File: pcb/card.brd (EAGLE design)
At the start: 69.5 x 40.6 mm, 21 parts, among them IC1 74HC14D, IC2 24LC256SN, Q1 BC817

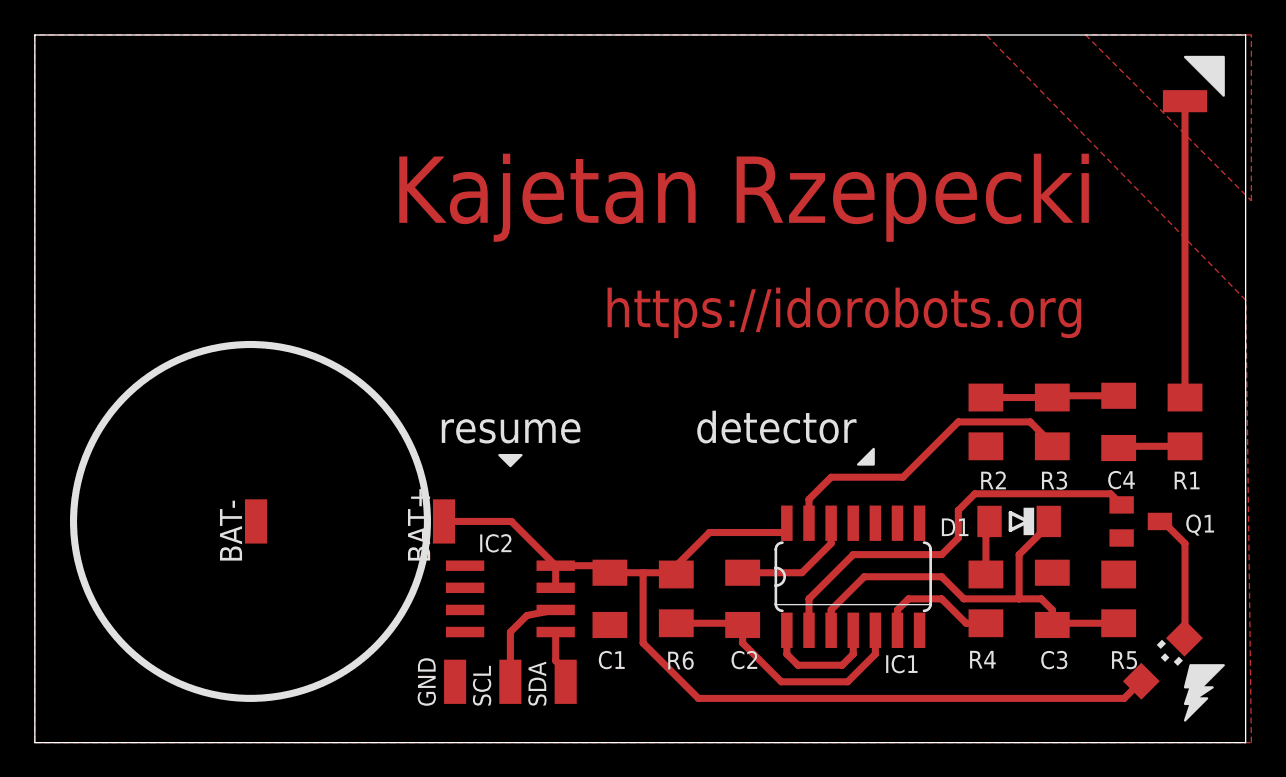
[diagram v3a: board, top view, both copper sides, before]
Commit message: Apparently 10M Ohm is as high as it gets for reasonable amount of money.
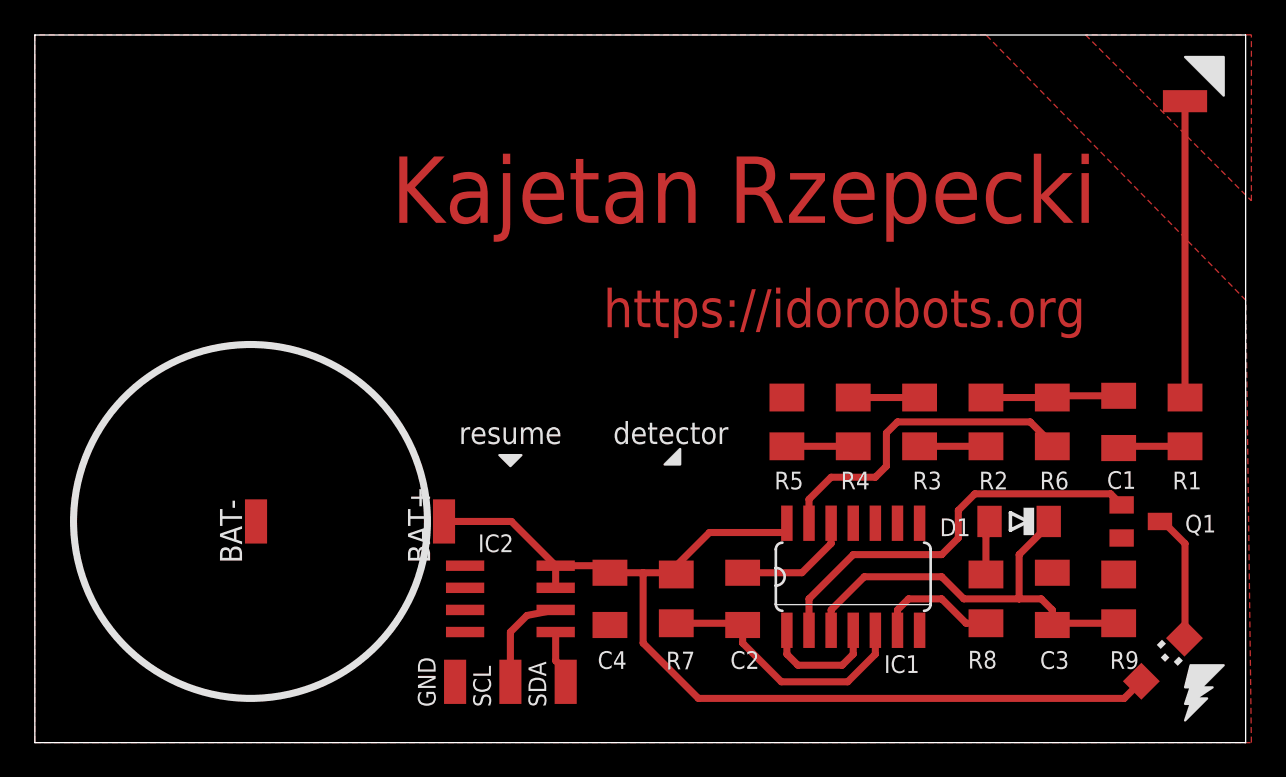
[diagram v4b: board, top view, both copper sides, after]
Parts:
- added R7, R9: 470k, resistor:M1206
- added R8: 100k, resistor:M1206
- R2: value 40M -> 10M
- R3, R5: value 470k -> 10M
- R4: value 100k -> 10M
- moved C1 30.9 mm to (62.2, 18.4)
- moved C4 30.9 mm to (33.0, 8.26)
- moved R6 23.9 mm to (58.4, 18.4)
- moved R5 21.6 mm to (43.2, 18.4), turned to 270 degrees
- moved R4 12.7 mm to (47.0, 18.4), turned to 90 degrees
- moved R3 7.62 mm to (50.8, 18.4), turned to 270 degrees
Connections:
- new net N$14: R2.1, R3.2
- new net N$15: R3.1, R4.2
- new net N$16: R4.1, R5.2
- net GND: now also C4.1, R5.1, R9.2; no longer C1.1, R2.1, R5.2
- net N$1: now also C1.1; no longer C4.1
- net N$2: now also C1.2, R6.2; no longer C4.2, R3.2
- net N$3: now also R6.1; no longer R3.1
- net N$5: now also R7.1; no longer R6.1
- net N$6: now also R8.2; no longer R4.2
- net N$7: now also R8.1; no longer R4.1
- net N$8: now also R9.1; no longer R5.1
- net VCC: now also C4.2, R7.2; no longer C1.2, R6.2
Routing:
- net N$16: track 0.00 -> 3.81 mm
- net N$14: track 0.00 -> 3.81 mm
- net N$15: track 0.00 -> 3.81 mm
- net N$3: track 18.8 -> 19.9 mm
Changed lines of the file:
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@@
 <setting verticaltext="up"/>
 </settings>
-<grid distance="0.3175" unitdist="mm" unit="mm" style="lines" multiple="1" display="no" altdistance="0.3175" altunitdist="mm" altunit="mm"/>
+<grid distance="0.635" unitdist="mm" unit="mm" style="lines" multiple="1" display="no" altdistance="0.3175" altunitdist="mm" altunit="mm"/>
 <layers>
 <layer number="1" name="Top" color="4" fill="1" visible="yes" active="yes"/>
@@
 <vertex x="27.94" y="16.51"/>
 </polygon>
-<text x="27.305" y="18.0975" size="1.778" layer="25" rot="R180" align="center">resume</text>
+<text x="27.305" y="17.78" size="1.27" layer="25" rot="R180" align="center">resume</text>
 <polygon width="0.127" layer="25">
-<vertex x="48.167003125" y="15.967996875"/>
-<vertex x="47.268975" y="15.96799375"/>
-<vertex x="48.167003125" y="16.866021875"/>
+<vertex x="37.054503125" y="15.967996875"/>
+<vertex x="36.156475" y="15.96799375"/>
+<vertex x="37.054503125" y="16.866021875"/>
 </polygon>
-<text x="42.545" y="18.0975" size="1.778" layer="25" rot="R180" align="center">detector</text>
+<text x="36.5125" y="17.78" size="1.27" layer="25" rot="R180" align="center">detector</text>
 </plain>
 <attributes>
@@
 </autorouter>
 <elements>
-<element name="C1" library="resistor" package="C1206K" value="10nF" x="33.02" y="8.255" smashed="yes" rot="R90">
+<element name="C4" library="resistor" package="C1206K" value="10nF" x="33.02" y="8.255" smashed="yes" rot="R90">
 <attribute name="NAME" x="33.985" y="5.25" size="1.016" layer="25" rot="R180"/>
 </element>
@@
 <attribute name="NAME" x="66.9925" y="15.5575" size="1.016" layer="25" rot="R180"/>
 </element>
-<element name="R2" library="resistor" package="M1206" value="40M" x="54.61" y="18.415" smashed="yes" rot="R90">
+<element name="R2" library="resistor" package="M1206" value="10M" x="54.61" y="18.415" smashed="yes" rot="R90">
 <attribute name="NAME" x="55.88" y="15.5575" size="1.016" layer="25" rot="R180"/>
 </element>
-<element name="R3" library="resistor" package="M1206" value="470k" x="58.42" y="18.415" smashed="yes" rot="R90">
+<element name="R6" library="resistor" package="M1206" value="470k" x="58.42" y="18.415" smashed="yes" rot="R90">
 <attribute name="NAME" x="59.3725" y="15.5575" size="1.016" layer="25" rot="R180"/>
 </element>
-<element name="R4" library="resistor" package="M1206" value="100k" x="54.61" y="8.255" smashed="yes" rot="R270">
+<element name="R8" library="resistor" package="M1206" value="100k" x="54.61" y="8.255" smashed="yes" rot="R270">
 <attribute name="NAME" x="55.245" y="5.2700625" size="1.016" layer="25" rot="R180"/>
 </element>
-<element name="R5" library="resistor" package="M1206" value="470k" x="62.23" y="8.255" smashed="yes" rot="R90">
+<element name="R9" library="resistor" package="M1206" value="470k" x="62.23" y="8.255" smashed="yes" rot="R90">
 <attribute name="NAME" x="63.39549375" y="5.251046875" size="1.016" layer="25" rot="R180"/>
 </element>
-<element name="R6" library="resistor" package="M1206" value="470k" x="36.83" y="8.255" smashed="yes" rot="R90">
+<element name="R7" library="resistor" package="M1206" value="470k" x="36.83" y="8.255" smashed="yes" rot="R90">
 <attribute name="NAME" x="37.910009375" y="5.222546875" size="1.016" layer="25" rot="R180"/>
 </element>
@@
 <attribute name="NAME" x="23.0125" y="2.045" size="1.016" layer="25" rot="R90"/>
 </element>
-<element name="C4" library="resistor" package="C1206K" value="10nF" x="62.23" y="18.415" smashed="yes" rot="R90">
+<element name="C1" library="resistor" package="C1206K" value="10nF" x="62.23" y="18.415" smashed="yes" rot="R90">
 <attribute name="NAME" x="63.23010625" y="15.5856" size="1.016" layer="25" rot="R180"/>
+</element>
+<element name="R3" library="resistor" package="M1206" value="10M" x="50.8" y="18.415" smashed="yes" rot="R270">
+<attribute name="NAME" x="52.07" y="15.5575" size="1.016" layer="25" rot="R180"/>
+</element>
+<element name="R4" library="resistor" package="M1206" value="10M" x="46.99" y="18.415" smashed="yes" rot="R90">
+<attribute name="NAME" x="47.9425" y="15.5575" size="1.016" layer="25" rot="R180"/>
+</element>
+<element name="R5" library="resistor" package="M1206" value="10M" x="43.18" y="18.415" smashed="yes" rot="R270">
+<attribute name="NAME" x="44.1325" y="15.5575" size="1.016" layer="25" rot="R180"/>
 </element>
 </elements>
@@
 <signal name="GND">
 <contactref element="IC1" pad="7"/>
-<contactref element="R2" pad="1"/>
 <contactref element="IC1" pad="11"/>
 <contactref element="IC1" pad="9"/>
-<contactref element="R5" pad="2"/>
+<contactref element="R9" pad="2"/>
 <contactref element="C3" pad="2"/>
 <contactref element="Q1" pad="E"/>
-<contactref element="C1" pad="1"/>
+<contactref element="C4" pad="1"/>
 <polygon width="0.4064" layer="1" isolate="0.4064" orphans="yes">
 <vertex x="0" y="40.64"/>
@@
 <contactref element="IC2" pad="4"/>
 <contactref element="GND" pad="1"/>
+<contactref element="R5" pad="1"/>
 </signal>
 <signal name="VCC">
 <contactref element="IC1" pad="14"/>
-<contactref element="R6" pad="2"/>
+<contactref element="R7" pad="2"/>
 <contactref element="LED" pad="A"/>
-<contactref element="C1" pad="2"/>
+<contactref element="C4" pad="2"/>
 <contactref element="BAT+" pad="1"/>
 <contactref element="IC2" pad="8"/>
@@
 <signal name="N$2">
 <contactref element="R2" pad="2"/>
-<contactref element="R3" pad="2"/>
-<contactref element="C4" pad="2"/>
+<contactref element="R6" pad="2"/>
+<contactref element="C1" pad="2"/>
 <wire x1="62.23" y1="19.915" x2="58.8375" y2="19.915" width="0.4064" layer="1"/>
 <wire x1="58.8375" y1="19.915" x2="58.42" y2="19.815" width="0.4064" layer="1"/>
@@
 </signal>
 <signal name="N$3">
-<contactref element="R3" pad="1"/>
+<contactref element="R6" pad="1"/>
 <contactref element="IC1" pad="13"/>
 <wire x1="44.45" y1="13.335" x2="44.45" y2="12.5984" width="0.4064" layer="1"/>
@@
 <wire x1="58.42" y1="17.015" x2="58.55" y2="17.015" width="0.4064" layer="1"/>
 <wire x1="58.55" y1="17.015" x2="57.15" y2="18.415" width="0.4064" layer="1"/>
-<wire x1="57.15" y1="18.415" x2="53.0225" y2="18.415" width="0.4064" layer="1"/>
-<wire x1="53.0225" y1="18.415" x2="49.8475" y2="15.24" width="0.4064" layer="1"/>
-<wire x1="49.8475" y1="15.24" x2="45.72" y2="15.24" width="0.4064" layer="1"/>
+<wire x1="45.72" y1="15.24" x2="48.26" y2="15.24" width="0.4064" layer="1"/>
+<wire x1="48.26" y1="15.24" x2="48.895" y2="15.875" width="0.4064" layer="1"/>
+<wire x1="48.895" y1="15.875" x2="48.895" y2="17.78" width="0.4064" layer="1"/>
+<wire x1="48.895" y1="17.78" x2="49.53" y2="18.415" width="0.4064" layer="1"/>
+<wire x1="49.53" y1="18.415" x2="57.15" y2="18.415" width="0.4064" layer="1"/>
 </signal>
 <signal name="N$4">
@@
 <contactref element="C2" pad="1"/>
 <contactref element="IC1" pad="5"/>
-<contactref element="R6" pad="1"/>
+<contactref element="R7" pad="1"/>
 <wire x1="36.83" y1="6.855" x2="40.54" y2="6.855" width="0.4064" layer="1"/>
 <wire x1="40.54" y1="6.855" x2="40.64" y2="6.755" width="0.4064" layer="1"/>
@@
 <signal name="N$6">
 <contactref element="IC1" pad="6"/>
-<contactref element="R4" pad="2"/>
+<contactref element="R8" pad="2"/>
 <wire x1="49.53" y1="6.4516" x2="49.53" y2="5.715" width="0.4064" layer="1"/>
 <wire x1="54.61" y1="6.855" x2="53.47" y2="6.855" width="0.4064" layer="1"/>
@@
 </signal>
 <signal name="N$7">
-<contactref element="R4" pad="1"/>
+<contactref element="R8" pad="1"/>
 <contactref element="D1" pad="A"/>
 <wire x1="54.61" y1="9.655" x2="54.61" y2="11.86" width="0.4064" layer="1"/>
@@
 <contactref element="D1" pad="C"/>
 <contactref element="IC1" pad="3"/>
-<contactref element="R5" pad="1"/>
+<contactref element="R9" pad="1"/>
 <contactref element="C3" pad="1"/>
 <wire x1="45.72" y1="7.62" x2="45.72" y2="6.4516" width="0.4064" layer="1"/>
@@
 <signal name="N$1">
 <contactref element="R1" pad="1"/>
-<contactref element="C4" pad="1"/>
+<contactref element="C1" pad="1"/>
 <wire x1="66.04" y1="17.015" x2="61.9125" y2="17.015" width="0.4064" layer="1"/>
 <wire x1="61.9125" y1="17.015" x2="62.23" y2="16.915" width="0.4064" layer="1"/>
 </signal>
+<signal name="N$14">
+<contactref element="R2" pad="1"/>
+<contactref element="R3" pad="2"/>
+<wire x1="54.61" y1="17.015" x2="50.8" y2="17.015" width="0.4064" layer="1"/>
+</signal>
+<signal name="N$15">
+<contactref element="R3" pad="1"/>
+<contactref element="R4" pad="2"/>
+<wire x1="50.8" y1="19.815" x2="46.99" y2="19.815" width="0.4064" layer="1"/>
+</signal>
+<signal name="N$16">
+<contactref element="R4" pad="1"/>
+<contactref element="R5" pad="2"/>
+<wire x1="46.99" y1="17.015" x2="43.18" y2="17.015" width="0.4064" layer="1"/>
+</signal>
 </signals>

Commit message: Improved the antenna.
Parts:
- ANT: value (none) -> TPB1,27; device wirepad:SMD1,27-2,54 -> testpad:B1,27
- moved ANT 2.48 mm to (67.6, 38.7), turned to 0 degrees
- moved GND 0.32 mm to (24.1, 3.17)
- moved SCL 0.32 mm to (27.3, 3.17)
- moved SDA 0.32 mm to (30.5, 3.17)
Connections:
- net ANT: now also ANT.TP; no longer ANT.1
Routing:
- net ANT: track 17.7 -> 76.9 mm
- removed copper zone on layer 1, net ANT
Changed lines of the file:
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@@
 <text x="60.325" y="26.035" size="2.1844" layer="29" rot="R180">https://idorobots.org</text>
 <polygon width="0.127" layer="25">
-<vertex x="66.04" y="39.37"/>
-<vertex x="68.2625" y="39.37"/>
-<vertex x="68.2625" y="37.1475"/>
+<vertex x="64.77" y="38.1"/>
+<vertex x="66.9925" y="38.1"/>
+<vertex x="66.9925" y="35.8775"/>
 </polygon>
 <polygon width="0.127" layer="25">
@@
 </polygon>
 <text x="36.5125" y="17.78" size="1.27" layer="25" rot="R180" align="center">detector</text>
+<wire x1="29.845" y1="18.0975" x2="30.1625" y2="18.415" width="0.127" layer="25"/>
 </plain>
 <attributes>
@@
 </element>
 <element name="R2" library="resistor" package="M1206" value="10M" x="54.61" y="18.415" smashed="yes" rot="R90">
-<attribute name="NAME" x="55.88" y="15.5575" size="1.016" layer="25" rot="R180"/>
+<attribute name="NAME" x="55.5625" y="15.5575" size="1.016" layer="25" rot="R180"/>
 </element>
 <element name="R6" library="resistor" package="M1206" value="470k" x="58.42" y="18.415" smashed="yes" rot="R90">
@@
 </element>
 <element name="R9" library="resistor" package="M1206" value="470k" x="62.23" y="8.255" smashed="yes" rot="R90">
-<attribute name="NAME" x="63.39549375" y="5.251046875" size="1.016" layer="25" rot="R180"/>
+<attribute name="NAME" x="63.07799375" y="5.251046875" size="1.016" layer="25" rot="R180"/>
 </element>
 <element name="R7" library="resistor" package="M1206" value="470k" x="36.83" y="8.255" smashed="yes" rot="R90">
 <attribute name="NAME" x="37.910009375" y="5.222546875" size="1.016" layer="25" rot="R180"/>
 </element>
-<element name="SDA" library="wirepad" package="SMD1,27-2,54" value="" x="30.48" y="3.4925" smashed="yes" rot="R180">
-<attribute name="VALUE" x="30.48" y="3.4925" size="0.0254" layer="27" rot="R180"/>
-<attribute name="NAME" x="29.3625" y="2.045" size="1.016" layer="25" rot="R90"/>
-</element>
-<element name="SCL" library="wirepad" package="SMD1,27-2,54" value="" x="27.305" y="3.4925" smashed="yes" rot="R180">
-<attribute name="VALUE" x="27.305" y="3.4925" size="0.0254" layer="27" rot="R180"/>
-<attribute name="NAME" x="26.1875" y="2.045" size="1.016" layer="25" rot="R90"/>
+<element name="SDA" library="wirepad" package="SMD1,27-2,54" value="" x="30.48" y="3.175" smashed="yes" rot="R180">
+<attribute name="VALUE" x="30.48" y="3.175" size="0.0254" layer="27" rot="R180"/>
+<attribute name="NAME" x="29.3625" y="1.7275" size="1.016" layer="25" rot="R90"/>
+</element>
+<element name="SCL" library="wirepad" package="SMD1,27-2,54" value="" x="27.305" y="3.175" smashed="yes" rot="R180">
+<attribute name="VALUE" x="27.305" y="3.175" size="0.0254" layer="27" rot="R180"/>
+<attribute name="NAME" x="26.1875" y="1.7275" size="1.016" layer="25" rot="R90"/>
 </element>
 <element name="BAT+" library="wirepad" package="SMD1,27-2,54" value="" x="23.495" y="12.7"/>
 <element name="BAT-" library="wirepad" package="SMD1,27-2,54" value="" x="12.7" y="12.7"/>
-<element name="ANT" library="wirepad" package="SMD1,27-2,54" value="" x="66.04" y="36.83" smashed="yes" rot="R90">
-<attribute name="VALUE" x="66.04" y="36.83" size="0.0254" layer="27" rot="R90"/>
-</element>
 <element name="IC2" library="microchip" package="SO-08" value="24LC256SN" x="27.305" y="8.255" smashed="yes" rot="R270">
 <attribute name="OC_FARNELL" value="9757996" x="27.305" y="8.255" size="1.016" layer="27" rot="R270" display="off"/>
@@
 <attribute name="NAME" x="25.447496875" y="10.937109375" size="1.016" layer="25"/>
 </element>
-<element name="GND" library="wirepad" package="SMD1,27-2,54" value="" x="24.13" y="3.4925" smashed="yes" rot="R180">
-<attribute name="VALUE" x="24.13" y="3.4925" size="0.0254" layer="27" rot="R180"/>
-<attribute name="NAME" x="23.0125" y="2.045" size="1.016" layer="25" rot="R90"/>
+<element name="GND" library="wirepad" package="SMD1,27-2,54" value="" x="24.13" y="3.175" smashed="yes" rot="R180">
+<attribute name="VALUE" x="24.13" y="3.175" size="0.0254" layer="27" rot="R180"/>
+<attribute name="NAME" x="23.0125" y="1.7275" size="1.016" layer="25" rot="R90"/>
 </element>
 <element name="C1" library="resistor" package="C1206K" value="10nF" x="62.23" y="18.415" smashed="yes" rot="R90">
@@
 </element>
 <element name="R3" library="resistor" package="M1206" value="10M" x="50.8" y="18.415" smashed="yes" rot="R270">
-<attribute name="NAME" x="52.07" y="15.5575" size="1.016" layer="25" rot="R180"/>
+<attribute name="NAME" x="51.7525" y="15.5575" size="1.016" layer="25" rot="R180"/>
 </element>
 <element name="R4" library="resistor" package="M1206" value="10M" x="46.99" y="18.415" smashed="yes" rot="R90">
@@
 <element name="R5" library="resistor" package="M1206" value="10M" x="43.18" y="18.415" smashed="yes" rot="R270">
 <attribute name="NAME" x="44.1325" y="15.5575" size="1.016" layer="25" rot="R180"/>
+</element>
+<element name="ANT" library="testpad" package="B1,27" value="TPB1,27" x="67.6275" y="38.735" smashed="yes">
+<attribute name="TP_SIGNAL_NAME" value="" x="66.9925" y="36.83" size="1" layer="37"/>
+<attribute name="VALUE" x="66.9925" y="37.973" size="0.0254" layer="27"/>
 </element>
 </elements>
@@
 <vertex x="0" y="0"/>
 <vertex x="69.85" y="0"/>
-<vertex x="69.5325" y="25.4"/>
-<vertex x="54.61" y="40.64"/>
+<vertex x="69.5325" y="24.765"/>
+<vertex x="53.6575" y="40.64"/>
 </polygon>
 <contactref element="BAT-" pad="1"/>
@@
 <wire x1="29.905" y1="7.62" x2="28.2575" y2="7.3025" width="0.4064" layer="1"/>
 <wire x1="28.2575" y1="7.3025" x2="27.305" y2="6.35" width="0.4064" layer="1"/>
-<wire x1="27.305" y1="6.35" x2="27.305" y2="3.4925" width="0.4064" layer="1"/>
+<wire x1="27.305" y1="6.35" x2="27.305" y2="3.175" width="0.4064" layer="1"/>
 </signal>
 <signal name="N$10">
@@
 <wire x1="29.905" y1="6.35" x2="29.905" y2="4.7025" width="0.4064" layer="1"/>
 <wire x1="29.905" y1="4.7025" x2="30.48" y2="4.1275" width="0.4064" layer="1"/>
-<wire x1="30.48" y1="4.1275" x2="30.48" y2="3.4925" width="0.4064" layer="1"/>
+<wire x1="30.48" y1="4.1275" x2="30.48" y2="3.175" width="0.4064" layer="1"/>
 </signal>
 <signal name="ANT">
-<polygon width="0.4064" layer="1" isolate="0.4064" orphans="yes" thermals="no">
-<vertex x="60.325" y="40.64"/>
-<vertex x="69.85" y="31.115"/>
-<vertex x="69.85" y="40.64"/>
-</polygon>
 <contactref element="R1" pad="2"/>
-<contactref element="ANT" pad="1"/>
-<wire x1="66.04" y1="36.83" x2="65.405" y2="36.83" width="0.4064" layer="1"/>
-<wire x1="66.04" y1="19.815" x2="66.04" y2="36.83" width="0.4064" layer="1"/>
+<wire x1="68.2625" y1="31.4325" x2="68.2625" y2="29.5275" width="0.4064" layer="1"/>
+<wire x1="68.2625" y1="29.5275" x2="58.42" y2="39.37" width="0.4064" layer="1"/>
+<wire x1="58.42" y1="39.37" x2="56.515" y2="39.37" width="0.4064" layer="1"/>
+<wire x1="56.515" y1="39.37" x2="68.2625" y2="27.6225" width="0.4064" layer="1"/>
+<wire x1="68.2625" y1="31.4325" x2="60.325" y2="39.37" width="0.4064" layer="1"/>
+<wire x1="60.325" y1="39.37" x2="62.23" y2="39.37" width="0.4064" layer="1"/>
+<wire x1="62.23" y1="39.37" x2="68.2625" y2="33.3375" width="0.4064" layer="1"/>
+<wire x1="68.2625" y1="33.3375" x2="68.2625" y2="35.2425" width="0.4064" layer="1"/>
+<wire x1="68.2625" y1="35.2425" x2="64.135" y2="39.37" width="0.4064" layer="1"/>
+<wire x1="68.2625" y1="27.6225" x2="68.2625" y2="23.1775" width="0.4064" layer="1"/>
+<wire x1="68.2625" y1="23.1775" x2="66.04" y2="20.955" width="0.4064" layer="1"/>
+<wire x1="66.04" y1="20.955" x2="66.04" y2="19.815" width="0.4064" layer="1"/>
+<contactref element="ANT" pad="TP"/>
+<wire x1="64.135" y1="39.37" x2="66.04" y2="39.37" width="0.4064" layer="1"/>
+<wire x1="66.04" y1="39.37" x2="67.31" y2="38.1" width="0.4064" layer="1"/>
+<wire x1="67.31" y1="38.1" x2="67.6275" y2="38.735" width="0.4064" layer="1"/>
 </signal>
 <signal name="N$1">
